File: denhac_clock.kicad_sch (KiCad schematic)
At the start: 20 parts, among them SW1 SET, SW2 CHANGE, U1 SN74HC595N, U2 TPIC6595, U3 LTC2723

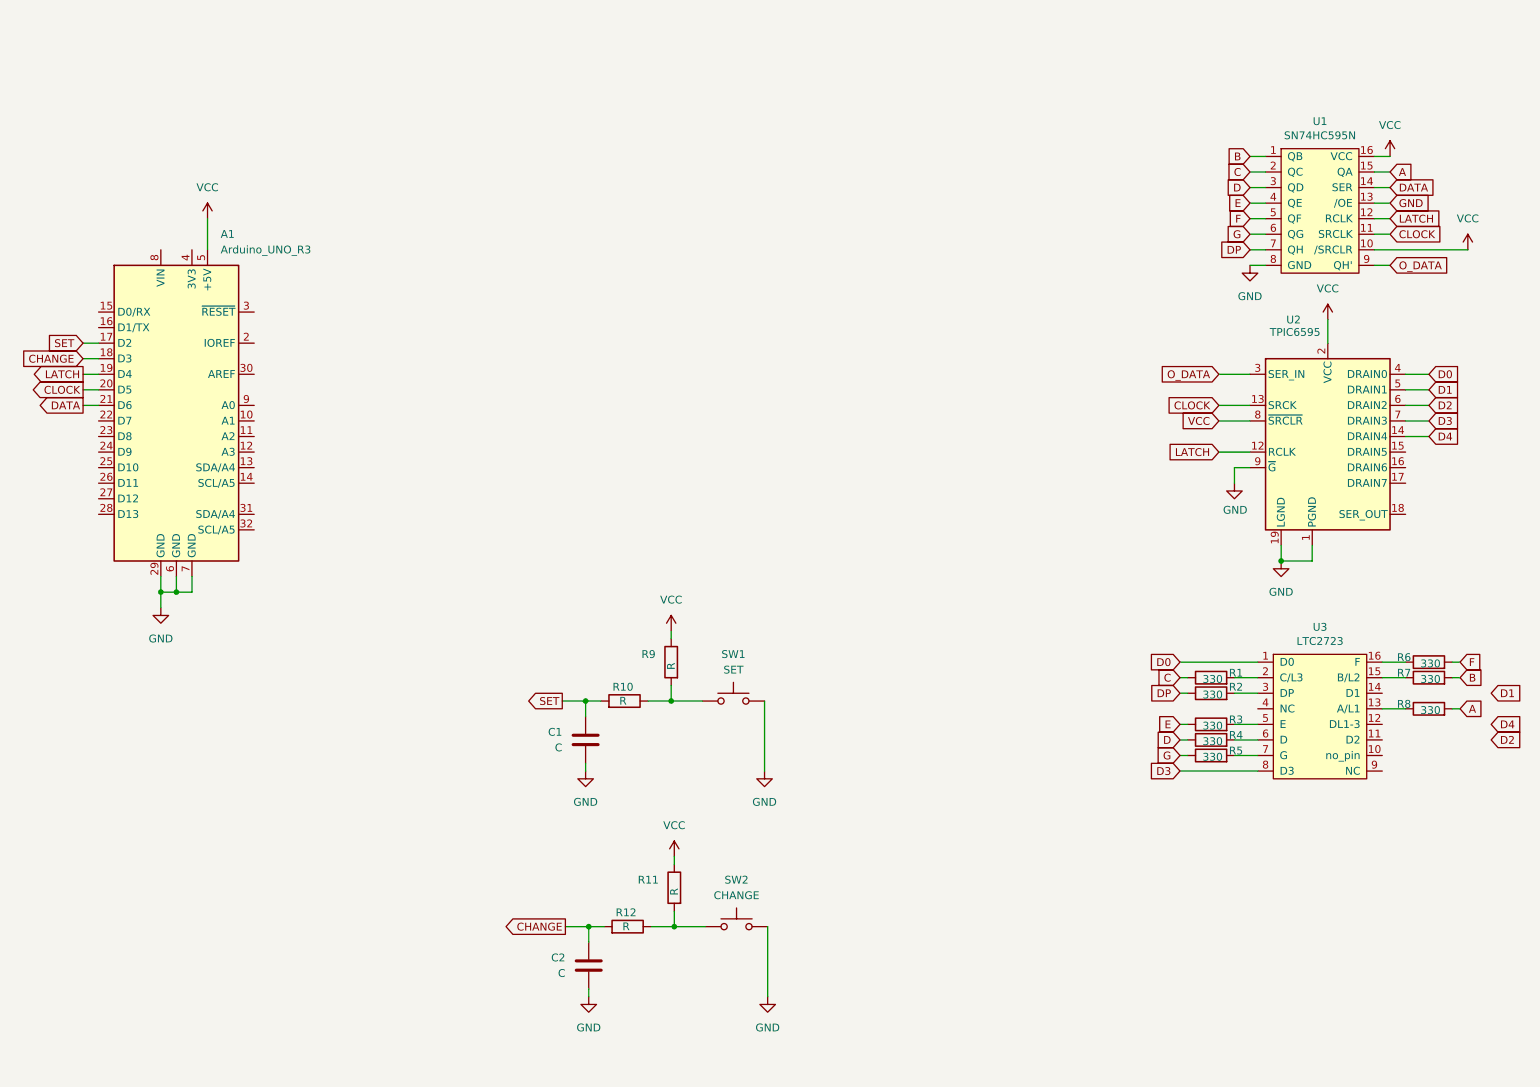
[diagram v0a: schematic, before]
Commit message: add DS1307 and footprint assignments
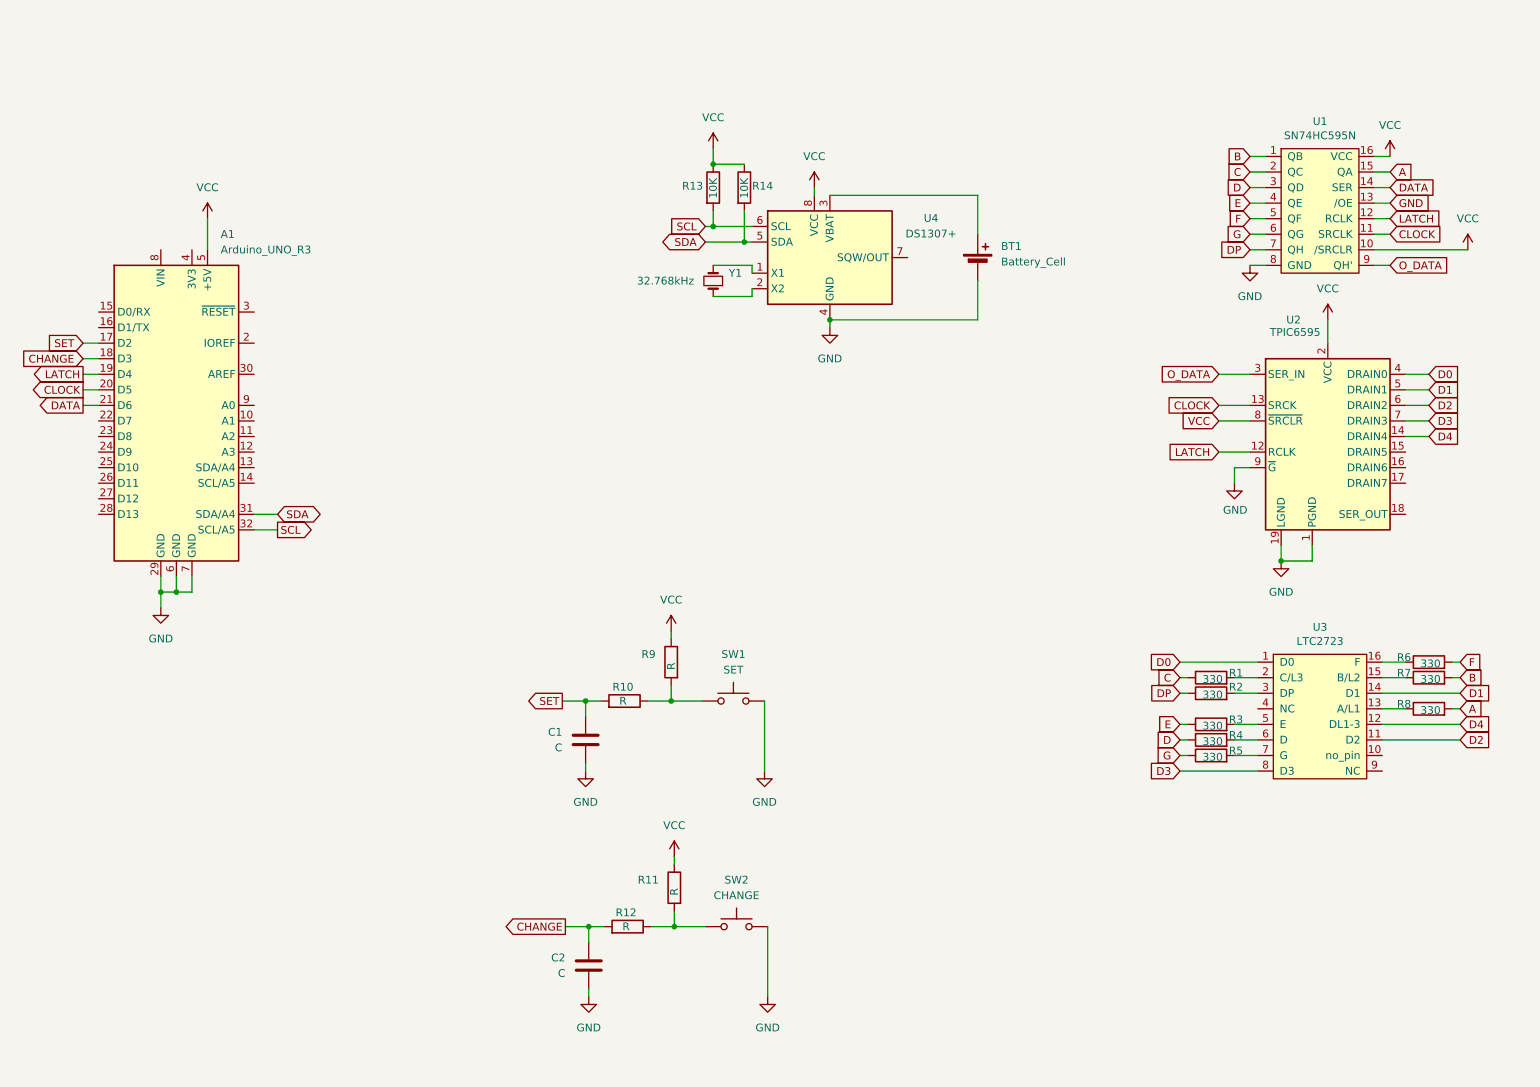
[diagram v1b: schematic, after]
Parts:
- added BT1: Battery_Cell, Battery:BatteryHolder_Multicomp_BC-2001_1x2032, symbol Device:Battery_Cell
- added R13, R14: 10K, Resistor_THT:R_Axial_DIN0207_L6.3mm_D2.5mm_P10.16mm_Horizontal, symbol Device:R
- added U4: DS1307+, Package_DIP:DIP-8_W7.62mm, symbol Timer_RTC:DS1307+
- added Y1: 32.768kHz, Crystal:Crystal_C38-LF_D3.0mm_L8.0mm_Horizontal, symbol Device:Crystal_Small
- C1, C2: footprint (none) -> Capacitor_THT:C_Disc_D4.3mm_W1.9mm_P5.00mm
- R1, R10, R11, R12, R2, R3, R4, R5, R6, R7, R8, R9: footprint (none) -> Resistor_THT:R_Axial_DIN0207_L6.3mm_D2.5mm_P10.16mm_Horizontal
- SW1, SW2: footprint (none) -> zgs:momentary_switch_2pin
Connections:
- net D1: now also U3.14 (D1)
- net D2: now also U3.11 (D2)
- net D4: now also U3.12 (DL1-3)
- net GND: now also BT1.2 (-), U4.4 (GND)
- net VCC: now also R13.1, R14.1, U4.8 (VCC)
- net SDA: now reaches A1.31 (SDA/A4)
- net SDA: now also R14.2, U4.5 (SDA)
- net SCL: now reaches A1.32 (SCL/A5)
- net SCL: now also R13.2, U4.6 (SCL)
- new net: BT1.1 (+), U4.3 (VBAT)
- new net: U4.1 (X1), Y1.2
- new net: U4.2 (X2), Y1.1

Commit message: replace single 4 segment display with 4 individual 1 segment displays
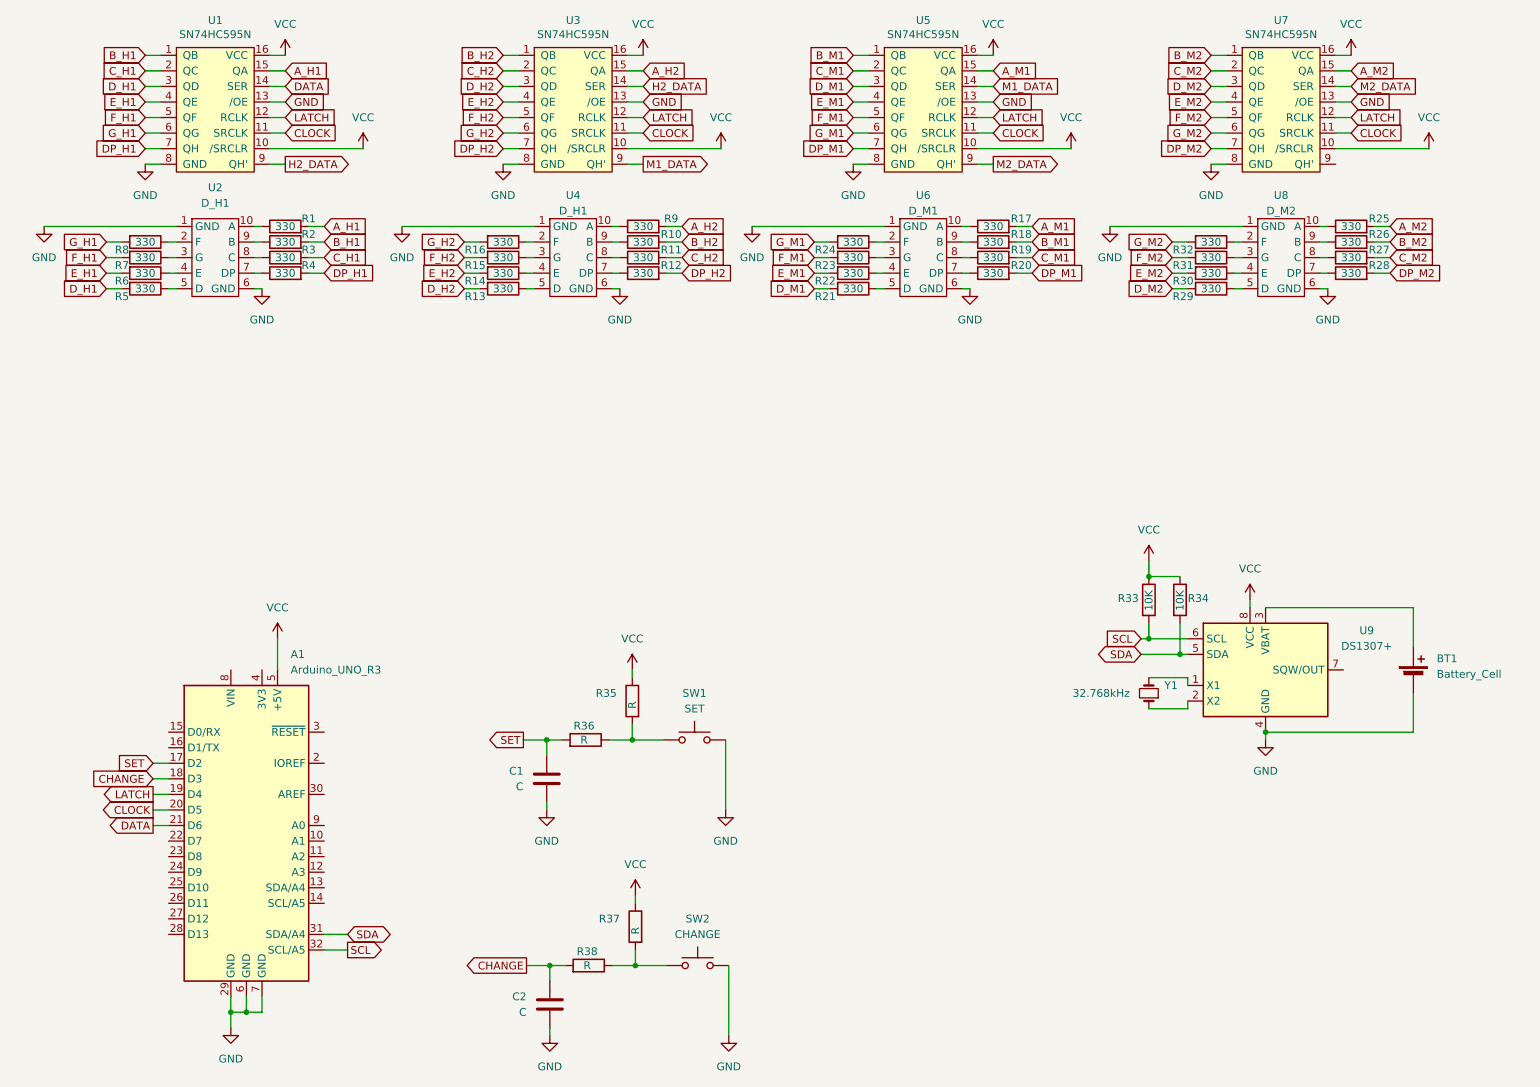
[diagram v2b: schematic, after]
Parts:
- removed U2: TPIC6595, Package_DIP:DIP-20_W7.62mm, symbol Interface_Expansion:TPIC6595
- removed U3: LTC2723, zgs:LTC2723, symbol four_digit_seven_segment_display_LTC2723-rescue:LTC2723-ZGS
- added R10, R11, R12, R13, R14, R15, R16, R17, R18, R19, R20, R21, R22, R23, R24, R25, R26, R27, R28, R29, R30, R31, R32, R9: 330, symbol Device:R
- added U2, U4: D_H1, symbol zgs:XL-DA3161SRBC
- added U3, U5, U7: SN74HC595N, Package_DIP:DIP-16_W7.62mm, symbol four_digit_seven_segment_display_LTC2723-rescue:SN74HC595N-ZGS
- added U6: D_M1, symbol zgs:XL-DA3161SRBC
- added U8: D_M2, symbol zgs:XL-DA3161SRBC
- R1, R2, R3, R4, R5, R6, R7, R8: footprint Resistor_THT:R_Axial_DIN0207_L6.3mm_D2.5mm_P10.16mm_Horizontal -> (none)
- renumbered R13 to R33, R14 to R34, R9 to R35, R10 to R36, R11 to R37, R12 to R38, U4 to U9
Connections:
- net CLOCK: now also U3.11 (SRCLK), U5.11 (SRCLK), U7.11 (SRCLK)
- net GND: now also U2.1 (GND), U2.6 (GND), U3.13 (/OE), U3.8 (GND), U4.1 (GND), U4.6 (GND), U5.13 (/OE), U5.8 (GND), U6.1 (GND), U6.6 (GND), U7.13 (/OE), U7.8 (GND), U8.1 (GND), U8.6 (GND)
- net LATCH: now also U3.12 (RCLK), U5.12 (RCLK), U7.12 (RCLK)
- net VCC: now also U3.10 (/SRCLR), U3.16 (VCC), U5.10 (/SRCLR), U5.16 (VCC), U7.10 (/SRCLR), U7.16 (VCC)
- net at R8.1: now also U2.2 (F)
- net at R7.1: now also U2.3 (G)
- net at R6.1: now also U2.4 (E)
- net A_H1: now reaches R1.2
- net A_H1: now also U1.15 (QA)
- net B_H1: now reaches R2.2
- net B_H1: now also U1.1 (QB)
- net C_H1: now reaches R3.2
- net C_H1: now also U1.2 (QC)
- net DP_H1: now reaches R4.2
- net DP_H1: now also U1.7 (QH)
- net D_H1: now reaches R5.2
- net D_H1: now also U1.3 (QD)
- net A renamed G_H1
- net G_H1: now also U1.6 (QG); no longer U1.15 (QA)
- net B renamed F_H1
- net F_H1: now also U1.5 (QF); no longer U1.1 (QB)
- net C: no longer names the net of R1.1
- net C: now also U2.10 (A); no longer U1.2 (QC)
- net D: no longer names the net of R4.1
- net D: now also U2.7 (DP); no longer U1.3 (QD)
- net DP: no longer names the net of R2.1
- net DP: now also U2.9 (B); no longer U1.7 (QH)
- net E: no longer names the net of R3.1
- net E: now also U2.8 (C); no longer U1.4 (QE)
- net F renamed E_H1
- net E_H1: now also U1.4 (QE); no longer U1.5 (QF)
- net G: no longer names the net of R5.1
- net G: now also U2.5 (D); no longer U1.6 (QG)
- net O_DATA renamed H2_DATA
- net H2_DATA: now also U3.14 (SER)
- new net: R13.1, U4.5 (D)
- new net: R29.1, U8.5 (D)
- new net: R16.1, U4.2 (F)
- new net: R21.1, U6.5 (D)
- new net: R25.1, U8.10 (A)
- new net: R26.1, U8.9 (B)
- new net: R14.1, U4.4 (E)
- new net: R30.1, U8.4 (E)
- new net: R17.1, U6.10 (A)
- new net: R20.1, U6.7 (DP)
- new net: R9.1, U4.10 (A)
- new net: R15.1, U4.3 (G)
- new net: R24.1, U6.2 (F)
- new net: R23.1, U6.3 (G)
- new net: R22.1, U6.4 (E)
- new net: R19.1, U6.8 (C)
- new net: R18.1, U6.9 (B)
- new net: R11.1, U4.8 (C)
- new net: R12.1, U4.7 (DP)
- new net: R10.1, U4.9 (B)
- new net: R32.1, U8.2 (F)
- new net: R31.1, U8.3 (G)
- new net: R28.1, U8.7 (DP)
- new net: R27.1, U8.8 (C)
- new net A_H2: R9.2, U3.15 (QA)
- new net A_M1: R17.2, U5.15 (QA)
- new net A_M2: R25.2, U7.15 (QA)
- new net B_H2: R10.2, U3.1 (QB)
- new net B_M1: R18.2, U5.1 (QB)
- new net B_M2: R26.2, U7.1 (QB)
- new net C_H2: R11.2, U3.2 (QC)
- new net C_M1: R19.2, U5.2 (QC)
- new net C_M2: R27.2, U7.2 (QC)
- new net DP_H2: R12.2, U3.7 (QH)
- new net DP_M1: R20.2, U5.7 (QH)
- new net DP_M2: R28.2, U7.7 (QH)
- new net D_H2: R13.2, U3.3 (QD)
- new net D_M1: R21.2, U5.3 (QD)
- new net D_M2: R29.2, U7.3 (QD)
- new net E_H2: R14.2, U3.4 (QE)
- new net E_M1: R22.2, U5.4 (QE)
- new net E_M2: R30.2, U7.4 (QE)
- new net F_H2: R15.2, U3.5 (QF)
- new net F_M1: R23.2, U5.5 (QF)
- new net F_M2: R31.2, U7.5 (QF)
- new net G_H2: R16.2, U3.6 (QG)
- new net G_M1: R24.2, U5.6 (QG)
- new net G_M2: R32.2, U7.6 (QG)
- new net M1_DATA: U3.9 (QH'), U5.14 (SER)
- new net M2_DATA: U5.9 (QH'), U7.14 (SER)
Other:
- moved on the sheet: A1, BT1, C1, C2, R33, R34, R35, R36, R37, R38, SW1, SW2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
